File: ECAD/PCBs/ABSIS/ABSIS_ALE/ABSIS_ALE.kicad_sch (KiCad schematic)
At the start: 29 parts, among them J1 Mini-Fit Jr. 2x03, J2 Mini-Fit Jr. 2x03, J3 PinHeader_2x06, J4 PinHeader_2x06, J5 PinHeader_1x06, J6 PinHeader_2x02, U1 MAX487EESA+T, U2 MIC5219

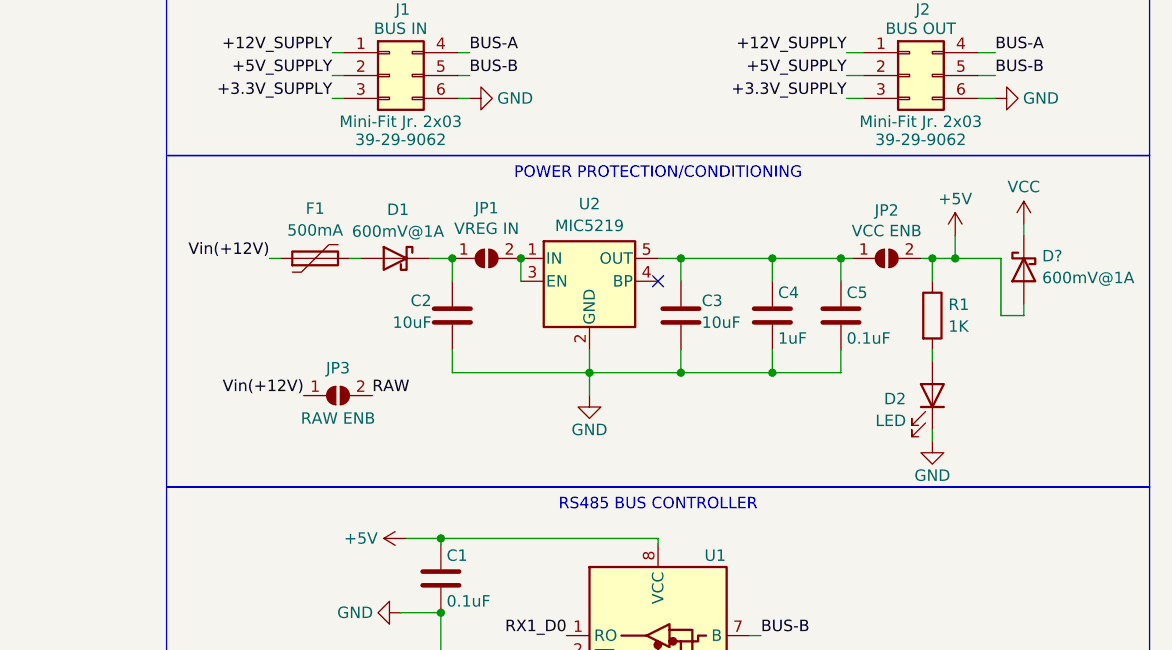
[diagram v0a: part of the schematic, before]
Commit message: Updated ABSIS ALE power stage
replaced LDO with a SMPS more suitable for handling the 12v to 5v drop.
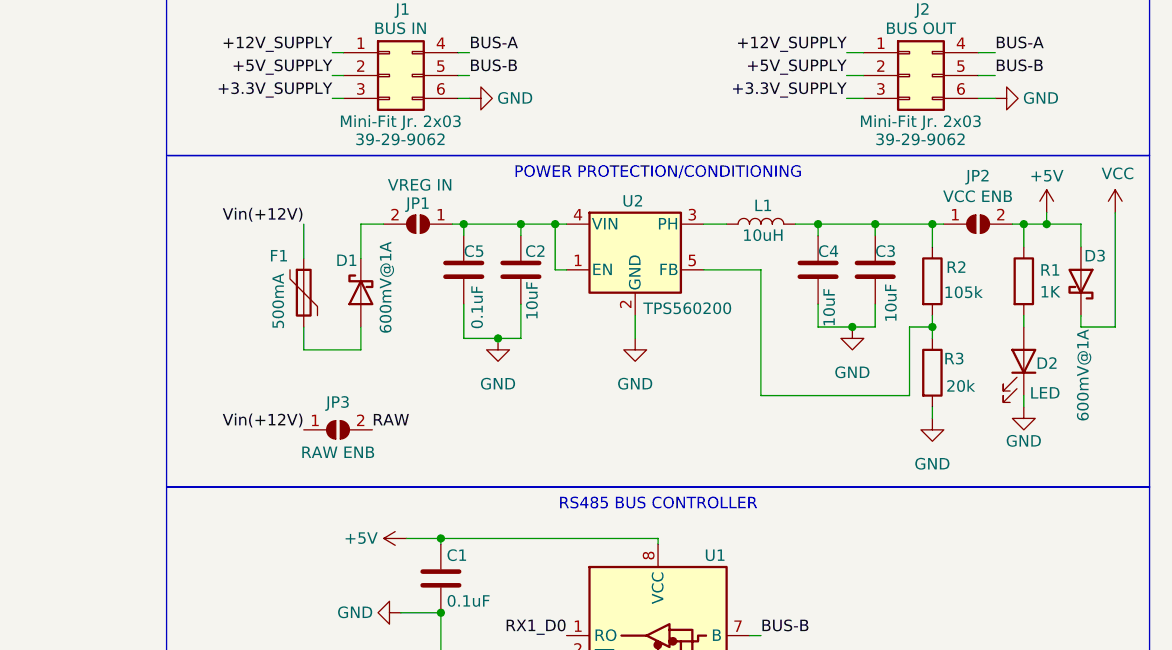
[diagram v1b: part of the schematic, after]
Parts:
- removed U2: MIC5219, Package_TO_SOT_SMD:SOT-23-5, symbol Regulator_Linear:MIC5219-5.0YM5
- added L1: 10uH, symbol Device:L
- added R2: 105k, symbol Device:R
- added R3: 20k, symbol Device:R
- added U2: TPS560200, Package_TO_SOT_SMD:SOT-23-5, symbol Regulator_Switching:TPS560200
- C4: value 1uF -> 10uF
- gave numbers to parts that had none: 1
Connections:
- net GND: now also R3.2, U2.2 (GND)
- net at C3.1, C4.1, JP2.1 (A): now also L1.2, R2.1; no longer C5.1
- net at C2.1, JP1.1 (A): now also C5.1, U2.1 (EN), U2.4 (VIN); no longer D1.1 (K)
- net at JP1.2 (B): now also D1.1 (K)
- new net: R2.2, R3.1, U2.5 (FB)
- new net: L1.1, U2.3 (PH)
- no-connect marks 1 -> 0
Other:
- moved on the sheet: C2, C3, C4, C5, D1, D2, D3, F1, JP1, JP2, JP3, R1
